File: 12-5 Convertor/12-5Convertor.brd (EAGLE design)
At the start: 28.6 x 42 mm, 7 parts, among them U1 LM2678

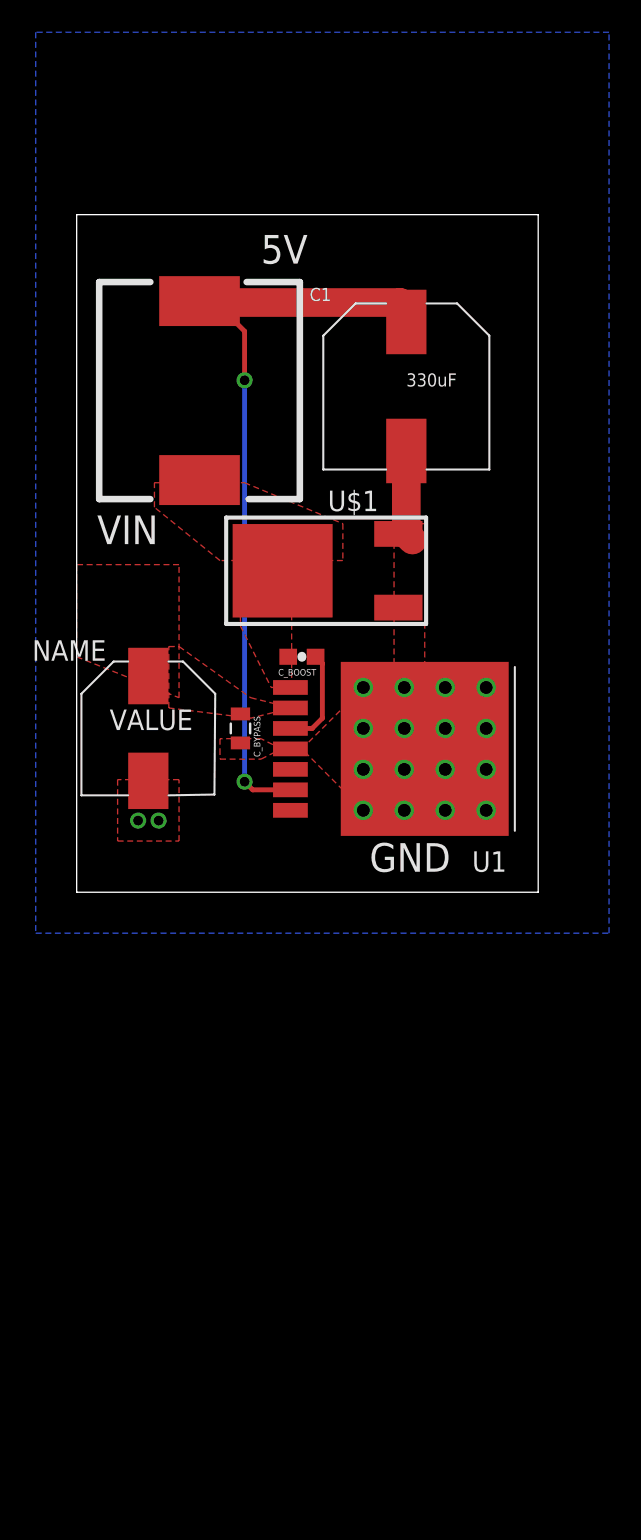
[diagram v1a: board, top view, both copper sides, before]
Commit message: Added Header Pins For testing
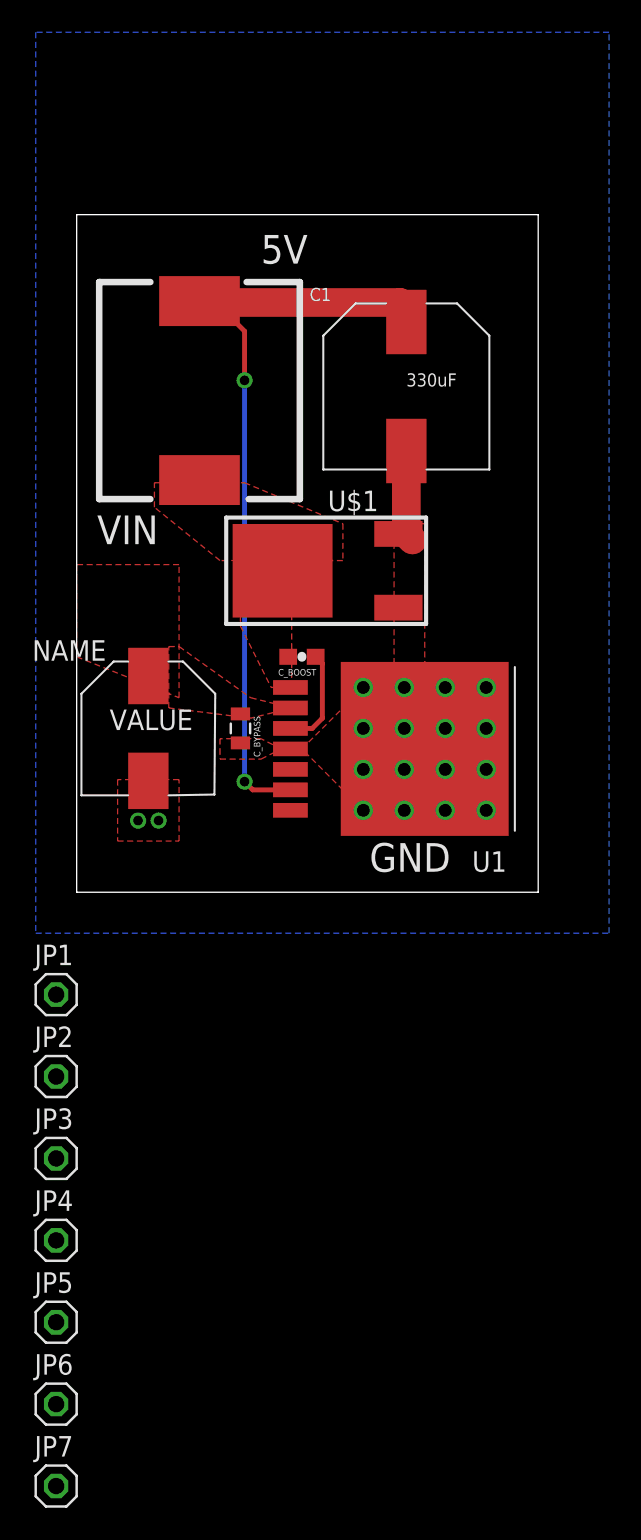
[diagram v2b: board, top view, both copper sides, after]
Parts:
- added JP1, JP2, JP3, JP4, JP5, JP6, JP7: (no value), pinhead:1X01
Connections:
- removed net 5V: C1.+, L1.P$2, U1.6
- removed net VIN: C_BYPASS.1, C_IN.+, U1.2
- new net +12V: C_BYPASS.1, C_IN.+, JP1.1, JP3.1, U1.2
- new net +5V: C1.+, JP6.1, JP7.1, L1.P$2, U1.6
- new net ON/OFF: JP4.1, U1.7
- net GND: now also JP2.1, JP5.1
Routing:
- net 5V: track 48.2 -> 0.00 mm, vias 2 -> 0
- net +5V: track 0.00 -> 46.8 mm, vias 0 -> 2
- added copper zone on layer 1, net +12V
- removed copper zone on layer 1, net VIN
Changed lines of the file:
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@@
 <element name="U$1" library="PowerComponents" package="DPAK-3" value="SWITCHMODE_SCHOTTKY" x="48.895" y="35.179"/>
 <element name="U1" library="PowerComponents" package="LM2678" value="LM2678" x="54.61" y="24.13" rot="R180"/>
+<element name="JP1" library="pinhead" package="1X01" value="" x="31.75" y="8.89"/>
+<element name="JP2" library="pinhead" package="1X01" value="" x="31.75" y="3.81"/>
+<element name="JP3" library="pinhead" package="1X01" value="" x="31.75" y="-1.27"/>
+<element name="JP4" library="pinhead" package="1X01" value="" x="31.75" y="-6.35"/>
+<element name="JP5" library="pinhead" package="1X01" value="" x="31.75" y="-11.43"/>
+<element name="JP6" library="pinhead" package="1X01" value="" x="31.75" y="-16.51"/>
+<element name="JP7" library="pinhead" package="1X01" value="" x="31.75" y="-21.59"/>
 </elements>
 <signals>
-<signal name="VIN">
-<contactref element="C_IN" pad="+"/>
-<contactref element="C_BYPASS" pad="1"/>
-<contactref element="U1" pad="2"/>
-<polygon width="0.254" layer="1" thermals="no">
-<vertex x="39.37" y="30.48"/>
-<vertex x="43.815" y="27.305"/>
-<vertex x="46.355" y="26.67"/>
-<vertex x="43.815" y="26.035"/>
-<vertex x="38.735" y="26.67"/>
-<vertex x="38.735" y="30.48"/>
-</polygon>
-<polygon width="0.254" layer="1" thermals="no">
-<vertex x="39.37" y="27.305"/>
-<vertex x="39.37" y="35.56"/>
-<vertex x="33.02" y="35.56"/>
-<vertex x="33.02" y="29.845"/>
-</polygon>
-</signal>
 <signal name="N$2">
 <contactref element="U1" pad="3"/>
@@
 <vertex x="37.846" y="39.116"/>
 </polygon>
-</signal>
-<signal name="5V">
-<contactref element="U1" pad="6"/>
-<contactref element="L1" pad="P$2"/>
-<contactref element="C1" pad="+"/>
-<wire x1="53.467" y1="50.609" x2="53.467" y2="51.435" width="1.778" layer="1"/>
-<wire x1="53.467" y1="51.435" x2="53.086" y2="51.816" width="1.778" layer="1"/>
-<wire x1="53.086" y1="51.816" x2="41.402" y2="51.816" width="1.778" layer="1"/>
-<wire x1="41.402" y1="51.816" x2="41.275" y2="51.689" width="1.778" layer="1"/>
-<wire x1="41.275" y1="51.689" x2="41.148" y2="51.562" width="1.778" layer="1"/>
-<wire x1="41.148" y1="51.562" x2="40.9829" y2="51.562" width="1.778" layer="1"/>
-<wire x1="40.9829" y1="51.562" x2="40.64" y2="51.9049" width="1.778" layer="1"/>
-<wire x1="41.402" y1="51.816" x2="41.402" y2="52.07" width="1.778" layer="1"/>
-<wire x1="46.2788" y1="21.59" x2="43.942" y2="21.59" width="0.3048" layer="1"/>
-<wire x1="43.942" y1="21.59" x2="43.434" y2="22.098" width="0.3048" layer="1"/>
-<via x="43.434" y="22.098" extent="1-16" drill="0.6"/>
-<wire x1="43.434" y1="22.098" x2="43.434" y2="46.99" width="0.3048" layer="16"/>
-<via x="43.434" y="46.99" extent="1-16" drill="0.6"/>
-<wire x1="43.434" y1="46.99" x2="43.434" y2="50.038" width="0.3048" layer="1"/>
-<wire x1="43.434" y1="50.038" x2="42.164" y2="51.308" width="0.3048" layer="1"/>
-<wire x1="42.164" y1="51.308" x2="41.656" y2="51.308" width="0.3048" layer="1"/>
-<wire x1="41.656" y1="51.308" x2="41.275" y2="51.689" width="0.3048" layer="1"/>
 </signal>
 <signal name="GND">
@@
 <wire x1="53.467" y1="42.609" x2="53.467" y2="37.465" width="1.778" layer="1"/>
 <wire x1="53.467" y1="37.465" x2="53.848" y2="37.084" width="1.778" layer="1"/>
+<contactref element="JP2" pad="1"/>
+<contactref element="JP5" pad="1"/>
+<wire x1="52.975" y1="37.464" x2="53.467" y2="37.465" width="0" layer="19" extent="1-1"/>
+<wire x1="52.975" y1="32.894" x2="53.848" y2="37.084" width="0" layer="19" extent="1-1"/>
+<wire x1="53.34" y1="27.94" x2="52.975" y2="32.894" width="0" layer="19" extent="1-1"/>
+<wire x1="55.88" y1="27.94" x2="53.34" y2="27.94" width="0" layer="19" extent="1-1"/>
+<wire x1="58.42" y1="27.94" x2="55.88" y2="27.94" width="0" layer="19" extent="1-1"/>
+<wire x1="58.42" y1="25.4" x2="58.42" y2="27.94" width="0" layer="19" extent="1-1"/>
+<wire x1="58.42" y1="22.86" x2="58.42" y2="25.4" width="0" layer="19" extent="1-1"/>
+<wire x1="55.88" y1="25.4" x2="55.88" y2="27.94" width="0" layer="19" extent="1-1"/>
+<wire x1="54.61" y1="24.13" x2="55.88" y2="25.4" width="0" layer="19" extent="1-1"/>
+<wire x1="53.34" y1="25.4" x2="54.61" y2="24.13" width="0" layer="19" extent="1-1"/>
+<wire x1="55.88" y1="22.86" x2="54.61" y2="24.13" width="0" layer="19" extent="1-1"/>
+<wire x1="53.34" y1="22.86" x2="54.61" y2="24.13" width="0" layer="19" extent="1-1"/>
+<wire x1="50.8" y1="27.94" x2="53.34" y2="27.94" width="0" layer="19" extent="1-1"/>
+<wire x1="58.42" y1="20.32" x2="58.42" y2="22.86" width="0" layer="19" extent="1-1"/>
+<wire x1="50.8" y1="25.4" x2="53.34" y2="25.4" width="0" layer="19" extent="1-1"/>
+<wire x1="55.88" y1="20.32" x2="55.88" y2="22.86" width="0" layer="19" extent="1-1"/>
+<wire x1="50.8" y1="22.86" x2="53.34" y2="22.86" width="0" layer="19" extent="1-1"/>
+<wire x1="53.34" y1="20.32" x2="53.34" y2="22.86" width="0" layer="19" extent="1-1"/>
+<wire x1="50.8" y1="20.32" x2="50.8" y2="22.86" width="0" layer="19" extent="1-1"/>
+<wire x1="46.2788" y1="24.13" x2="50.8" y2="25.4" width="0" layer="19" extent="1-1"/>
+<wire x1="43.18" y1="24.5" x2="46.2788" y2="24.13" width="0" layer="19" extent="1-1"/>
+<wire x1="37.465" y1="22.15" x2="43.18" y2="24.5" width="0" layer="19" extent="1-1"/>
+<wire x1="38.1" y1="19.685" x2="37.465" y2="22.15" width="0" layer="19" extent="1-1"/>
+<wire x1="36.83" y1="19.685" x2="38.1" y2="19.685" width="0" layer="19" extent="1-1"/>
+<wire x1="31.75" y1="3.81" x2="36.83" y2="19.685" width="0" layer="19" extent="1-1"/>
+<wire x1="31.75" y1="-11.43" x2="31.75" y2="3.81" width="0" layer="19" extent="1-1"/>
+</signal>
+<signal name="ON/OFF">
+<contactref element="JP4" pad="1"/>
+<contactref element="U1" pad="7"/>
+<wire x1="31.75" y1="-6.35" x2="46.2788" y2="20.32" width="0" layer="19" extent="1-1"/>
+</signal>
+<signal name="+12V">
+<contactref element="C_BYPASS" pad="1"/>
+<contactref element="C_IN" pad="+"/>
+<contactref element="U1" pad="2"/>
+<contactref element="JP3" pad="1"/>
+<contactref element="JP1" pad="1"/>
+<polygon width="0.254" layer="1" thermals="no">
+<vertex x="39.37" y="30.48"/>
+<vertex x="43.815" y="27.305"/>
+<vertex x="46.355" y="26.67"/>
+<vertex x="43.815" y="26.035"/>
+<vertex x="38.735" y="26.67"/>
+<vertex x="38.735" y="30.48"/>
+</polygon>
+<polygon width="0.254" layer="1" thermals="no">
+<vertex x="39.37" y="27.305"/>
+<vertex x="39.37" y="35.56"/>
+<vertex x="33.02" y="35.56"/>
+<vertex x="33.02" y="29.845"/>
+</polygon>
+<wire x1="43.18" y1="26.3" x2="46.2788" y2="26.67" width="0" layer="19" extent="1-1"/>
+<wire x1="37.465" y1="28.65" x2="43.18" y2="26.3" width="0" layer="19" extent="1-1"/>
+<wire x1="31.75" y1="8.89" x2="37.465" y2="28.65" width="0" layer="19" extent="1-1"/>
+<wire x1="31.75" y1="-1.27" x2="31.75" y2="8.89" width="0" layer="19" extent="1-1"/>
+</signal>
+<signal name="+5V">
+<contactref element="L1" pad="P$2"/>
+<contactref element="C1" pad="+"/>
+<contactref element="U1" pad="6"/>
+<wire x1="53.467" y1="51.435" x2="53.086" y2="51.816" width="1.778" layer="1"/>
+<wire x1="53.086" y1="51.816" x2="41.402" y2="51.816" width="1.778" layer="1"/>
+<wire x1="41.402" y1="51.816" x2="41.275" y2="51.689" width="1.778" layer="1"/>
+<wire x1="41.275" y1="51.689" x2="41.148" y2="51.562" width="1.778" layer="1"/>
+<wire x1="41.148" y1="51.562" x2="40.9829" y2="51.562" width="1.778" layer="1"/>
+<wire x1="41.402" y1="51.816" x2="41.402" y2="52.07" width="1.778" layer="1"/>
+<wire x1="46.2788" y1="21.59" x2="43.942" y2="21.59" width="0.3048" layer="1"/>
+<wire x1="43.942" y1="21.59" x2="43.434" y2="22.098" width="0.3048" layer="1"/>
+<via x="43.434" y="22.098" extent="1-16" drill="0.6"/>
+<wire x1="43.434" y1="22.098" x2="43.434" y2="46.99" width="0.3048" layer="16"/>
+<via x="43.434" y="46.99" extent="1-16" drill="0.6"/>
+<wire x1="43.434" y1="46.99" x2="43.434" y2="50.038" width="0.3048" layer="1"/>
+<wire x1="43.434" y1="50.038" x2="42.164" y2="51.308" width="0.3048" layer="1"/>
+<wire x1="42.164" y1="51.308" x2="41.656" y2="51.308" width="0.3048" layer="1"/>
+<wire x1="41.656" y1="51.308" x2="41.275" y2="51.689" width="0.3048" layer="1"/>
+<contactref element="JP6" pad="1"/>
+<contactref element="JP7" pad="1"/>
+<wire x1="53.467" y1="51.435" x2="53.467" y2="50.609" width="0" layer="19" extent="1-1"/>
+<wire x1="40.64" y1="51.9049" x2="40.9829" y2="51.562" width="0" layer="19" extent="1-1"/>
+<wire x1="31.75" y1="-16.51" x2="43.942" y2="21.59" width="0" layer="19" extent="1-1"/>
+<wire x1="31.75" y1="-21.59" x2="31.75" y2="-16.51" width="0" layer="19" extent="1-1"/>
 </signal>
 </signals>

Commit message: Cleaned the 12-5 buck regulator
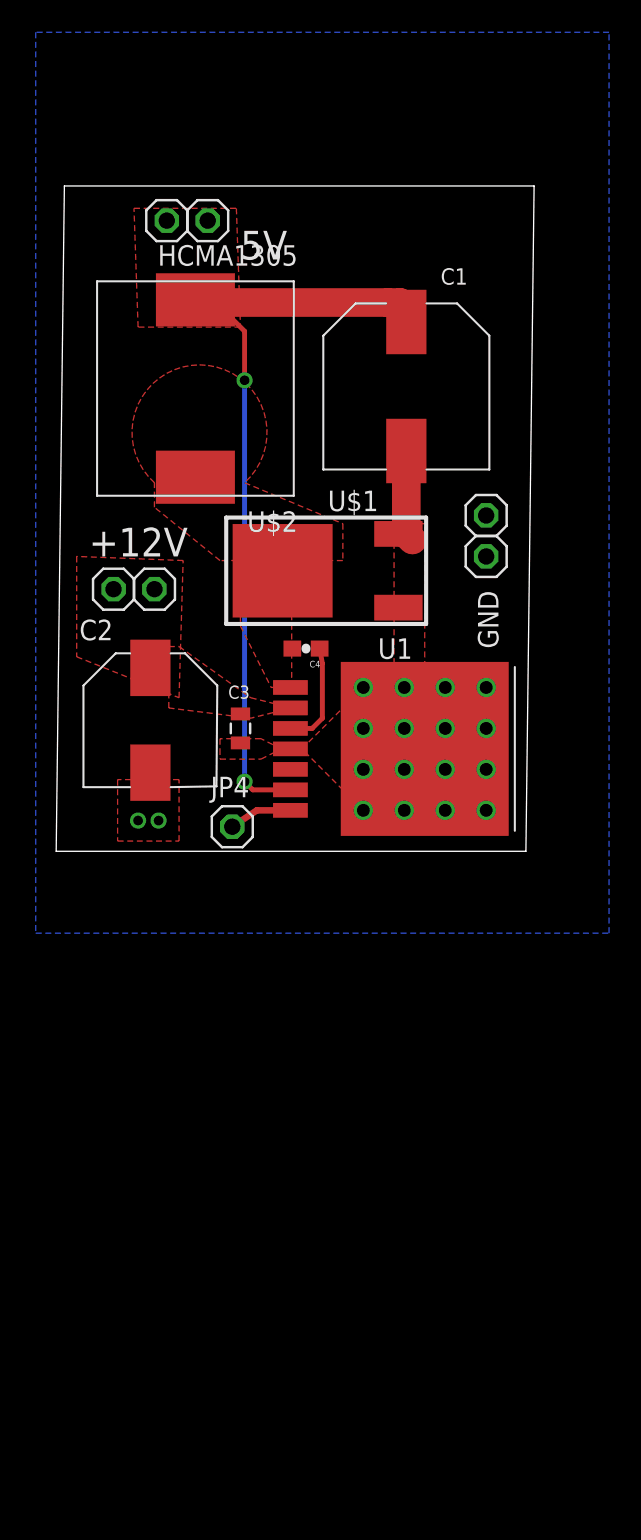
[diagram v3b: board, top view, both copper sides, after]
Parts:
- removed C_BOOST: 0.01uF, SparkFun-Passives:0603-CAP
- removed C_IN: C-ALUMINUM(47UF), PowerComponents:CPOL-US(8.3_8.3MM)
- removed L1: 22uH, DiscreteComponents:SRP1265A
- added C2: C-ALUMINUM(47UF), PowerComponents:CPOL-US(8.3_8.3MM)
- added C4: 0.01uF, SparkFun-Passives:0603-CAP
- added U$2: HCMA1305, DiscreteComponents:HCMA1305
- moved JP7 78.8 mm to (38.6, 56.9)
- moved JP6 74.0 mm to (41.1, 56.9)
- moved JP5 56.7 mm to (58.4, 38.6)
- moved JP2 41.9 mm to (58.4, 36.1)
- moved JP3 35.8 mm to (37.8, 34.0)
- moved JP4 27.9 mm to (42.7, 19.3)
- moved JP1 25.4 mm to (35.3, 34.0)
- renumbered C_BYPASS to C3
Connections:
- net +12V: now also C2.+; no longer C_IN.+
- net +5V: now also U$2.P$2; no longer L1.P$2
- net GND: now also C2.-; no longer C_IN.-
- net N$2: now also C4.1; no longer C_BOOST.1
- net N$3: now also C4.2, U$2.P$1; no longer C_BOOST.2, L1.P$1
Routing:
- net +5V: track 46.8 -> 53.1 mm
- net ON/OFF: track 0.00 -> 3.91 mm
- added copper zone on layer 1, net +5V
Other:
- board size 28.6 x 42 mm -> 29.6 x 41.3 mm
- board text added: "+12V"
- board text removed: "VIN"
